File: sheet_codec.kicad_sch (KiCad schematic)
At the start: 17 parts, among them J3 Carrier LEFT 1-7, J4 Carrier RIGHT 1-7, U1 ES8389

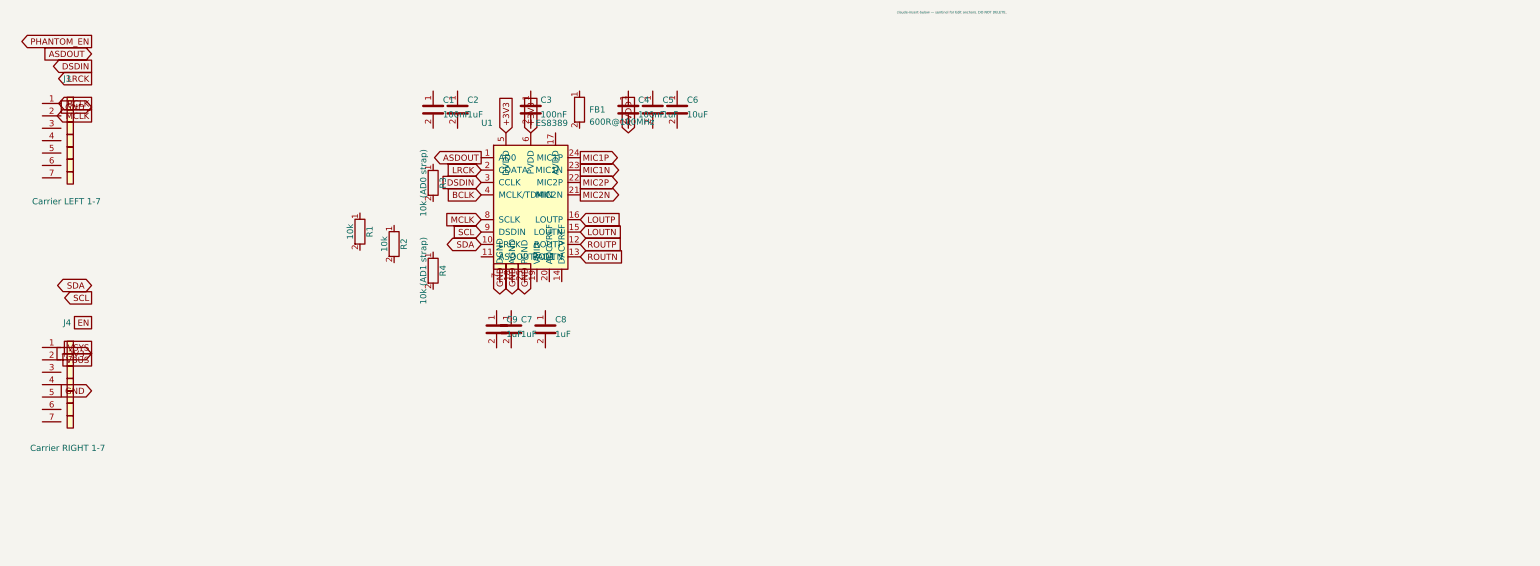
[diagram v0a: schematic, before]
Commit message: design: full iteration since init — codec, phantom/PoE, LDO, BOM, fab
First substantive commit since init; captures the entire design
iteration and quiets KiCad churn in-repo.

Codec / PCB
- ES8389: custom QFN-24 0.35mm land pattern (ES8389_QFN24_P0.35mm)
- Corrected mirror-reversed codec I2C/I2S pins
- Un-mirrored all B.Cu footprints that imported un-flipped
  (U1, OK1, Q1, D2, D6-D8 + silk)
- Re-coupled schematic to PCB netlist -> IN SYNC

Phantom / PoE
- F1 -> 1812L010/60DR (100mA hold / 60V, true 1812)
- Q1 -> Si2325DS (150V) for PoE++ margin
- Added SW1 SS-12D00-G3 slide switch = manual phantom enable (frees GPIO15)
- D8/R15/R16 phantom-present LED rework
- Confirmed PoE tap: BD1/BD2 (MB10F) -> VDD/VSS -> J5 pin 1/2

Power / connectors
- Added low-noise analog LDO U2 TPS7A2033 (+C21/C22): +5V -> +3V3_A -> AVDD
- J1 -> Neutrik NCJ6FA-H switched combo (+ 3D model)

Project
- BOM: single source of truth BOM.csv (JLCPCB-uploadable); removed BOM.md
- Added fab/ outputs (gerbers, drill, CPL) and tools/ (check_sync.py, relabel_sch.py)
- .gitignore: ignore KiCad churn (*.kicad_prl, *-drc.rpt, *-erc.rpt, backups) + local docs
- Untrack scramble_hat-erc.rpt (now ignored)
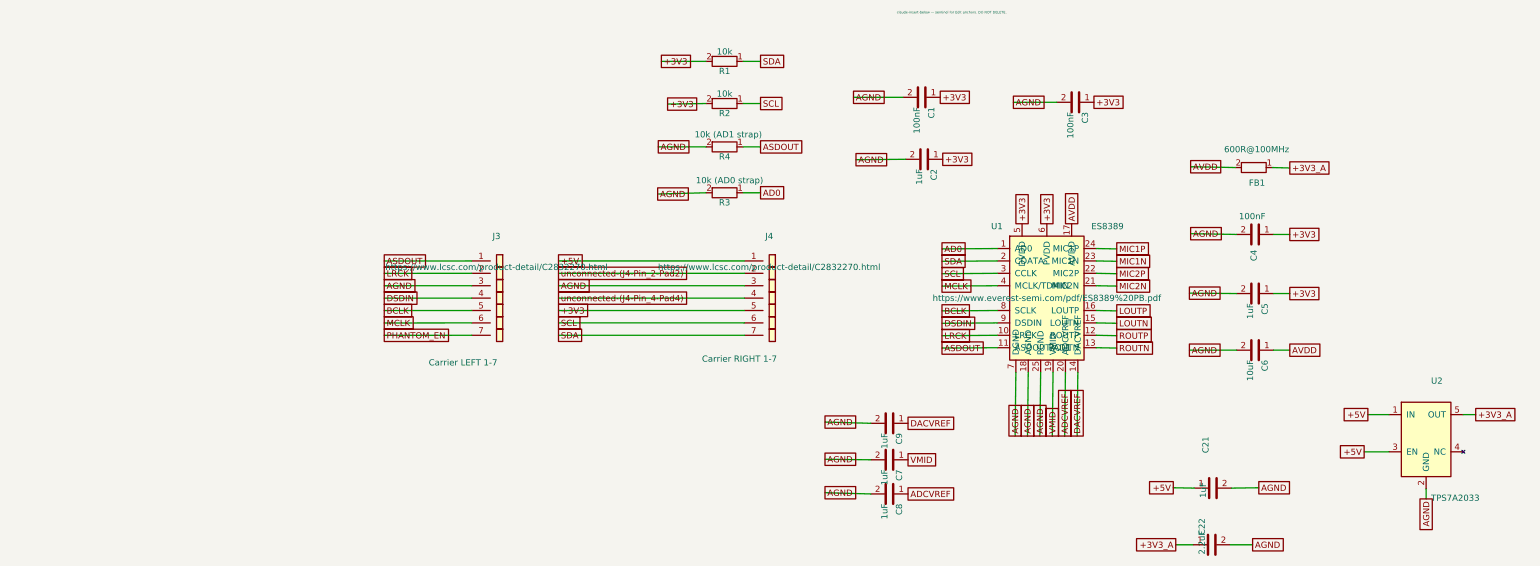
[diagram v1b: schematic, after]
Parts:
- added C21: 1uF, Capacitor_SMD:C_0402_1005Metric, symbol scramble_hat:C
- added C22: 2.2uF, Capacitor_SMD:C_0402_1005Metric, symbol scramble_hat:C
- added U2: TPS7A2033, Package_TO_SOT_SMD:SOT-23-5, symbol scramble_hat:TPS7A2033
- U1: footprint Package_DFN_QFN:QFN-24-1EP_3x3mm_P0.4mm_EP1.75x1.6mm -> scramble_hat:ES8389_QFN24_P0.35mm
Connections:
- net +3V3: now also C1.1, C2.1, C3.1, C4.1, C5.1, J4.5 (Pin_5), R1.2, R2.2
- net ASDOUT: now also J3.1 (Pin_1), R4.1, U1.11 (ASDOUT/AD1); no longer U1.1 (AD0)
- net AVDD: now also C6.1, FB1.2, U1.17 (AVDD)
- net BCLK: now also J3.5 (Pin_5), U1.8 (SCLK); no longer U1.4 (MCLK/TDMIN)
- net DSDIN: now also J3.4 (Pin_4), U1.9 (DSDIN); no longer U1.3 (CCLK)
- net LRCK: now also J3.2 (Pin_2), U1.10 (LRCK); no longer U1.2 (CDATA)
- net MCLK: now also J3.6 (Pin_6), U1.4 (MCLK/TDMIN); no longer U1.8 (SCLK)
- net PHANTOM_EN: now also J3.7 (Pin_7)
- net SCL: now also J4.6 (Pin_6), R2.1, U1.3 (CCLK); no longer U1.9 (DSDIN)
- net SDA: now also J4.7 (Pin_7), R1.1, U1.2 (CDATA); no longer U1.10 (LRCK)
- net +3V3_A: now reaches FB1.1
- net +3V3_A: now also C22.1, U2.5 (OUT)
- net +5V: now reaches J4.1 (Pin_1)
- net +5V: now also C21.1, U2.1 (IN), U2.3 (EN)
- net unconnected-(J4-Pin_2-Pad2): now reaches J4.2 (Pin_2)
- net AGND: now reaches J4.3 (Pin_3)
- net AGND: now also C1.2, C2.2, C3.2, C4.2, C5.2, C6.2, C7.2, C8.2, C9.2, J3.3 (Pin_3), R3.2, R4.2, U1.18 (AGND), U1.25 (PGND), U1.7 (DGND), C21.2, C22.2, U2.2 (GND)
- net unconnected-(J4-Pin_4-Pad4): now reaches J4.4 (Pin_4)
- net DACVREF: now reaches C9.1
- net DACVREF: now also U1.14 (DACVREF)
- net VMID: now reaches U1.19 (VMID)
- net VMID: now also C7.1
- net ADCVREF: now reaches U1.20 (ADCVREF)
- net ADCVREF: now also C8.1
- net AD0: now reaches R3.1
- net AD0: now also U1.1 (AD0)
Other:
- moved on the sheet: C1, C2, C3, C4, C5, C6, C7, C8, C9, FB1, J3, J4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
